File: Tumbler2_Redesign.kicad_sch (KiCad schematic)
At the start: 60 parts, among them J1 Conn_01x04, J2 Conn_01x06, J3 Conn_01x06, J4 USB_C_Receptacle_USB2.0_16P, J5 USB_C_Receptacle_USB2.0_16P, J6 Conn_01x04, Q1 BC817, Q2 BC817, SW1 SW_Push, SW2 SW_Push, SW3 SW_Push, U1 AP63203WU, U2 ESP32-S3-WROOM-1, U3 CP2102N-A02-GQFN28R, U4 AP63205WU, U6 USBLC6-2SC6, U7 USBLC6-2SC6

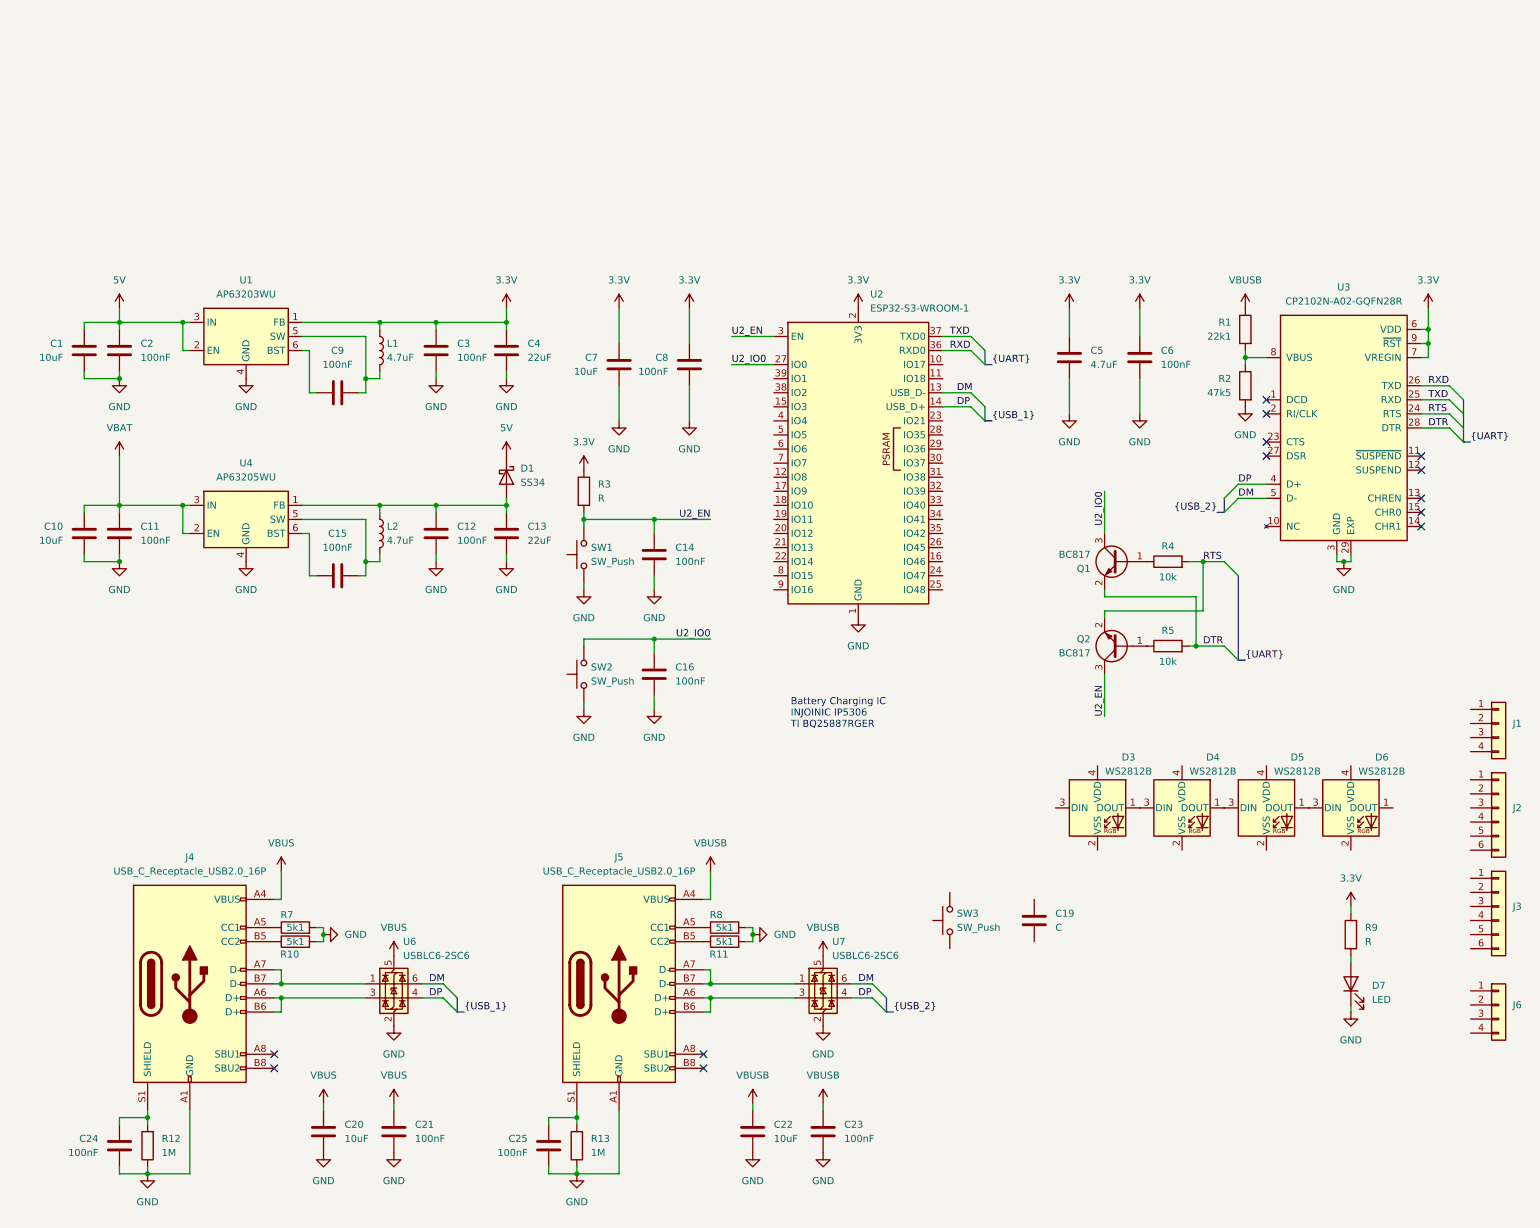
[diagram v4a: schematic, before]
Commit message: Add IMU and motor driver
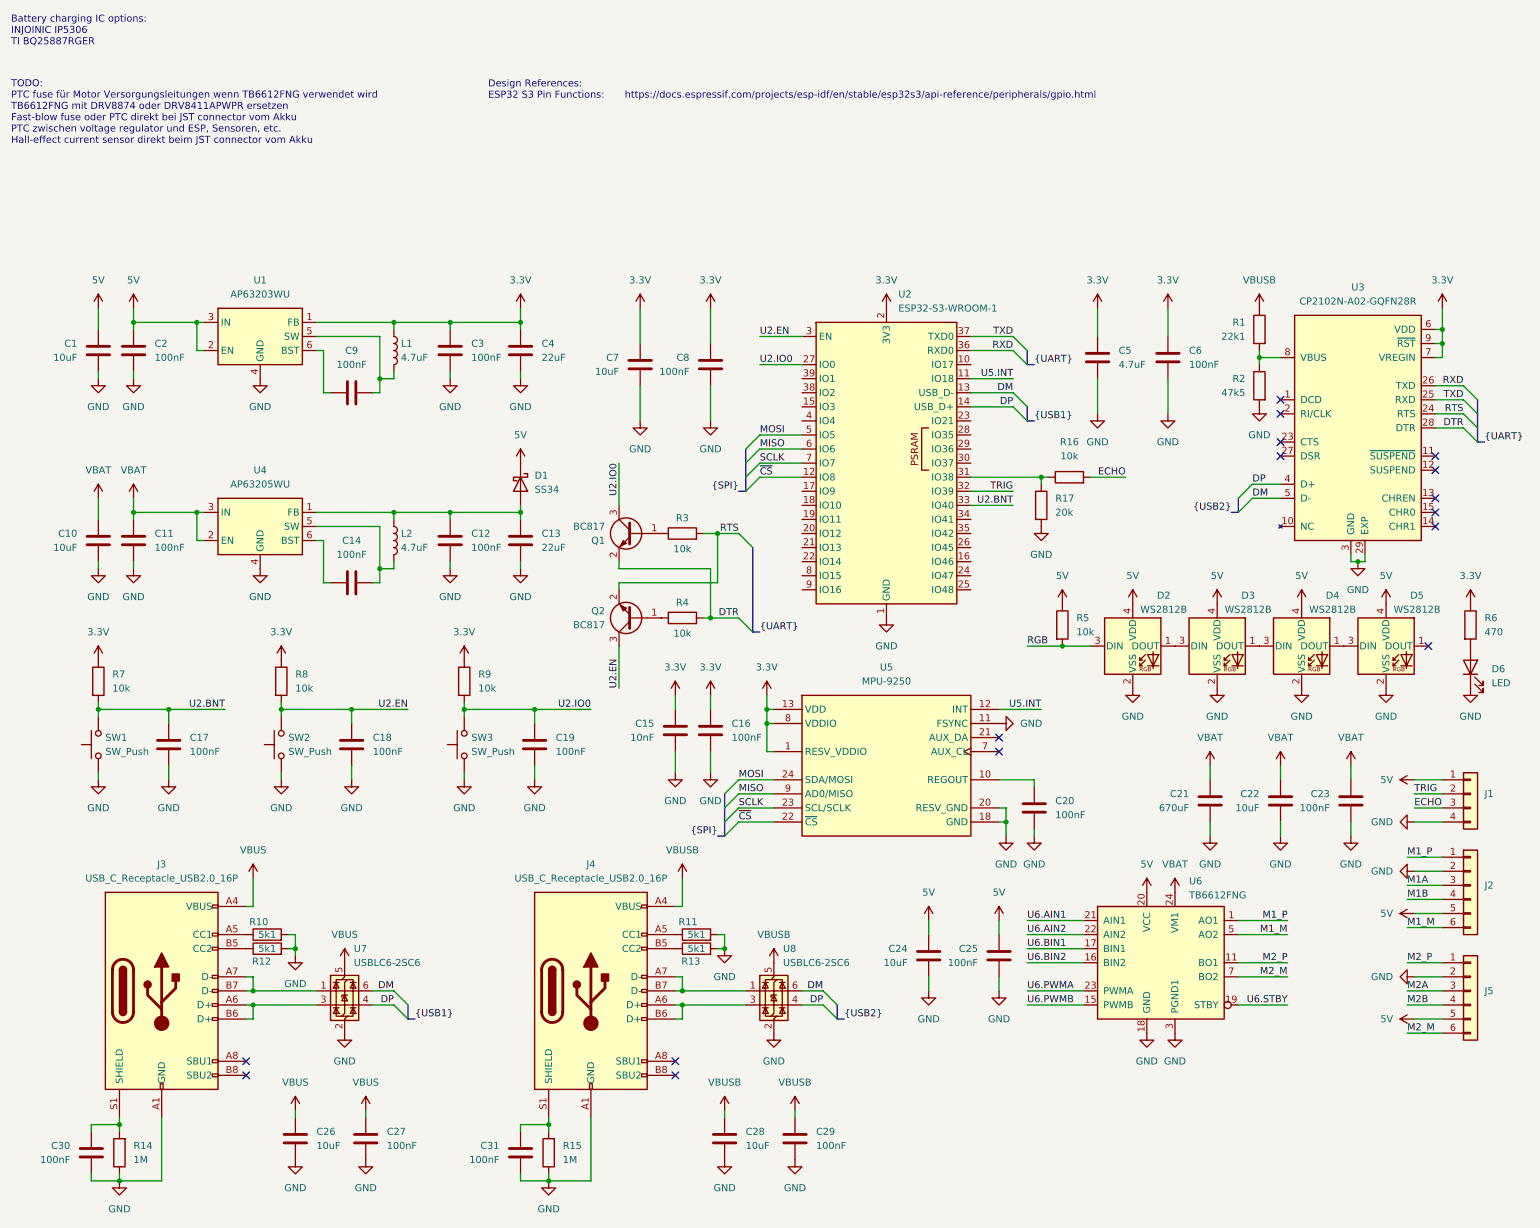
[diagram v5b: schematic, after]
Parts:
- removed C19: C, symbol Device:C
- removed J3: Conn_01x06, symbol Connector_Generic:Conn_01x06
- removed J6: Conn_01x04, symbol Connector_Generic:Conn_01x04
- removed SW3: SW_Push, symbol Switch:SW_Push
- added C15: 10nF, symbol Device:C
- added C16, C17, C20, C23, C25: 100nF, symbol Device:C
- added C21: 670uF, symbol Device:C
- added C22, C24: 10uF, symbol Device:C
- added J5: Conn_01x06, symbol Connector_Generic:Conn_01x06
- added R16, R5, R7, R9: 10k, symbol Device:R
- added R17: 20k, symbol Device:R
- added SW1: SW_Push, symbol Switch:SW_Push
- added U5: MPU-9250, Sensor_Motion:InvenSense_QFN-24_3x3mm_P0.4mm, symbol Sensor_Motion:MPU-9250
- added U6: TB6612FNG, Package_SO:SSOP-24_5.3x8.2mm_P0.65mm, symbol Driver_Motor:TB6612FNG
- D1: LSCS Part No. (none) -> C8678; Product_Link https://www.lcsc.com/product-detail/C8678.html -> (none)
- R6: renamed from R9; value R -> 470
- R8: renamed from R3; value R -> 10k
- U2: LSCS Part No. (none) -> C2913202
- renumbered C15 to C14, C14 to C18, C16 to C19, C20 to C26, C21 to C27, C22 to C28, C23 to C29, C24 to C30, C25 to C31, D3 to D2, D4 to D3, D5 to D4, D6 to D5, D7 to D6, J4 to J3, J5 to J4, R7 to R10, R8 to R11, R10 to R12, R11 to R13, R12 to R14, R13 to R15, R4 to R3, R5 to R4, SW1 to SW2, SW2 to SW3, U6 to U7, U7 to U8
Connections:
- net 3.3V: now also C15.1, C16.1, R7.1, R9.1, U5.1 (RESV_VDDIO), U5.13 (VDD), U5.8 (VDDIO)
- net 5V: now also D2.4 (VDD), D3.4 (VDD), D4.4 (VDD), D5.4 (VDD), J1.1 (Pin_1), J2.5 (Pin_5), C24.1, C25.1, J5.5 (Pin_5), R5.1, U6.20 (VCC)
- net GND: now also D2.2 (VSS), D3.2 (VSS), D4.2 (VSS), D5.2 (VSS), J1.4 (Pin_4), J2.2 (Pin_2), C15.2, C16.2, C17.2, C20.2, C21.2, C22.2, C23.2, C24.2, C25.2, J5.2 (Pin_2), R17.2, SW1.1, U5.11 (FSYNC), U5.18 (GND), U5.20 (RESV_GND), U6.10 (PGND2), U6.18 (GND), U6.3 (PGND1), U6.4 (PGND1), U6.9 (PGND2)
- net VBAT: now also C21.1, C22.1, C23.1, U6.13 (VM2), U6.14 (VM3), U6.24 (VM1)
- net TRIG: now reaches J1.2 (Pin_2)
- net TRIG: now also U2.32 (IO39)
- net ECHO: now reaches J1.3 (Pin_3)
- net ECHO: now also R16.2
- net U5.INT: now reaches U2.11 (IO18)
- net U5.INT: now also U5.12 (INT)
- net ~{CS}: now reaches U2.12 (IO8)
- net ~{CS}: now also U5.22 (~{CS})
- net at U2.31 (IO38): now also R16.1, R17.1
- net U2.BNT: now reaches U2.33 (IO40)
- net U2.BNT: now also C17.1, R7.2, SW1.2
- net MOSI: now reaches U2.5 (IO5)
- net MOSI: now also U5.24 (SDA/MOSI)
- net MISO: now reaches U2.6 (IO6)
- net MISO: now also U5.9 (AD0/MISO)
- net SCLK: now reaches U2.7 (IO7)
- net SCLK: now also U5.23 (SCL/SCLK)
- net RGB: now reaches D2.3 (DIN)
- net RGB: now also R5.2
- net M1_P: now reaches J2.1 (Pin_1)
- net M1_P: now also U6.1 (AO1), U6.2 (AO1)
- net M1A: now reaches J2.3 (Pin_3)
- net M1B: now reaches J2.4 (Pin_4)
- net M1_M: now reaches J2.6 (Pin_6)
- net M1_M: now also U6.5 (AO2), U6.6 (AO2)
- net U2_EN renamed U2.EN
- net U2_IO0 renamed U2.IO0
- net U2.IO0: now also R9.2
- new net: C20.1, U5.10 (REGOUT)
- new net M2A: J5.3 (Pin_3)
- new net M2B: J5.4 (Pin_4)
- new net M2_M: J5.6 (Pin_6), U6.7 (BO2), U6.8 (BO2)
- new net M2_P: J5.1 (Pin_1), U6.11 (BO1), U6.12 (BO1)
- new net U6.AIN1: U6.21 (AIN1)
- new net U6.AIN2: U6.22 (AIN2)
- new net U6.BIN1: U6.17 (BIN1)
- new net U6.BIN2: U6.16 (BIN2)
- new net U6.PWMA: U6.23 (PWMA)
- new net U6.PWMB: U6.15 (PWMB)
- new net U6.STBY: U6.19 (STBY)
- no-connect marks 13 -> 16
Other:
- note added: "Battery charging IC options: INJOINIC IP5306 TI BQ25887RGER"
- note added: "Design References: ESP32 S3 Pin Functions:"
- note added: "TODO: PTC fuse für Motor Versorgungsleitungen wenn TB6612FNG verwendet wird TB6612FNG mit DRV8874 oder DRV8411APWPR ersetzen Fast-blow fuse oder PTC direkt bei JST connector vom Akku PTC zwischen voltage regulator und ESP, Sensoren, etc. Hall-effect current sensor direkt beim JST connector vom Akku"
- note added: "https://docs.espressif.com/projects/esp-idf/en/stable/esp32s3/api-reference/peripherals/gpio.html"
- note removed: "Battery Charging IC INJOINIC IP5306 TI BQ25887RGER"
- moved on the sheet: C1, C10, C11, C12, C13, C14, C18, C19, C2, C26, C27, C28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

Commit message: Move to hierarchical design
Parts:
- removed C1, C10, C22, C24, C26, C28, C7: 10uF, symbol Device:C
- removed C11, C12, C14, C16, C17, C18, C19, C2, C20, C23, C25, C27, C29, C3, C30, C31, C6, C8, C9: 100nF, symbol Device:C
- removed C13, C4: 22uF, symbol Device:C
- removed C15: 10nF, symbol Device:C
- removed C21: 670uF, symbol Device:C
- removed C5: 4.7uF, symbol Device:C
- removed D1: SS34, Diode_SMD:D_SMA, symbol Diode:SS34
- removed D2, D3, D4, D5: WS2812B, LED_SMD:LED_WS2812B-2020_PLCC4_2.0x2.0mm, symbol LED:WS2812B-2020
- removed D6: LED, symbol Device:LED
- removed J1: Conn_01x04, symbol Connector_Generic:Conn_01x04
- removed J2, J5: Conn_01x06, symbol Connector_Generic:Conn_01x06
- removed J3, J4: USB_C_Receptacle_USB2.0_16P, symbol Connector:USB_C_Receptacle_USB2.0_16P
- removed L1, L2: 4.7uF, symbol Device:L
- removed Q1, Q2: BC817, Package_TO_SOT_SMD:SOT-23, symbol Transistor_BJT:BC817
- removed R1: 22k1, symbol Device:R
- removed R10, R11, R12, R13: 5k1, symbol Device:R
- removed R14, R15: 1M, symbol Device:R
- removed R16, R3, R4, R5, R7, R8, R9: 10k, symbol Device:R
- removed R17: 20k, symbol Device:R
- removed R2: 47k5, symbol Device:R
- removed R6: 470, symbol Device:R
- removed SW1, SW2, SW3: SW_Push, symbol Switch:SW_Push
- removed U1: AP63203WU, Package_TO_SOT_SMD:TSOT-23-6, symbol Regulator_Switching:AP63203WU
- removed U2: ESP32-S3-WROOM-1, RF_Module:ESP32-S3-WROOM-1, symbol RF_Module:ESP32-S3-WROOM-1
- removed U3: CP2102N-A02-GQFN28R, Package_DFN_QFN:QFN-28-1EP_5x5mm_P0.5mm_EP3.35x3.35mm, symbol Tumbler2:CP2102N-A02-GQFN28R
- removed U4: AP63205WU, Package_TO_SOT_SMD:TSOT-23-6, symbol Regulator_Switching:AP63205WU
- removed U5: MPU-9250, Sensor_Motion:InvenSense_QFN-24_3x3mm_P0.4mm, symbol Sensor_Motion:MPU-9250
- removed U6: TB6612FNG, Package_SO:SSOP-24_5.3x8.2mm_P0.65mm, symbol Driver_Motor:TB6612FNG
- removed U7, U8: USBLC6-2SC6, Package_TO_SOT_SMD:SOT-23-6, symbol Power_Protection:USBLC6-2SC6
- added H1, H2, H3, H4: MountingHole_Pad, MountingHole:MountingHole_3mm_Pad, symbol Mechanical:MountingHole_Pad
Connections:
- net GND: now also H1.1, H2.1, H3.1, H4.1
- no-connect marks 16 -> 0
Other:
- added sheet MCU (mcu.kicad_sch)
- added sheet Motor Driver (motor_driver.kicad_sch)
- added sheet Pin Headers (pin_headers.kicad_sch)
- added sheet Power Supply (power_supply.kicad_sch)
- added sheet Sensors (sensors.kicad_sch)
- added sheet USB-C Connectors (usb_c_connector.kicad_sch)
- title: (none) -> Tumbler 2 Redesign

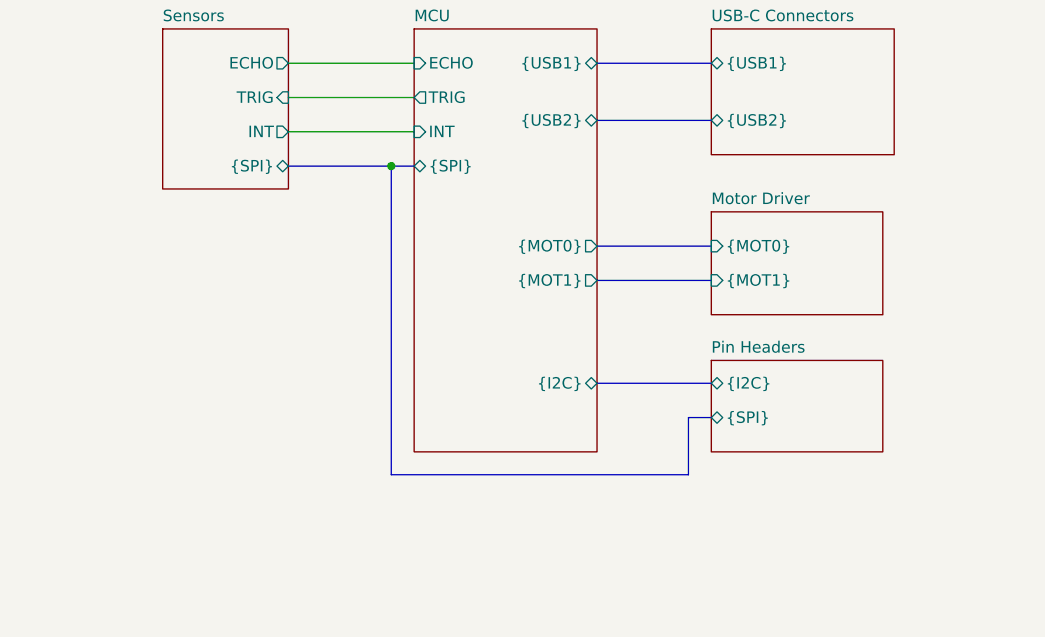
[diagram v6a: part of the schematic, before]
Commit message: Replace schottky with ideal diode
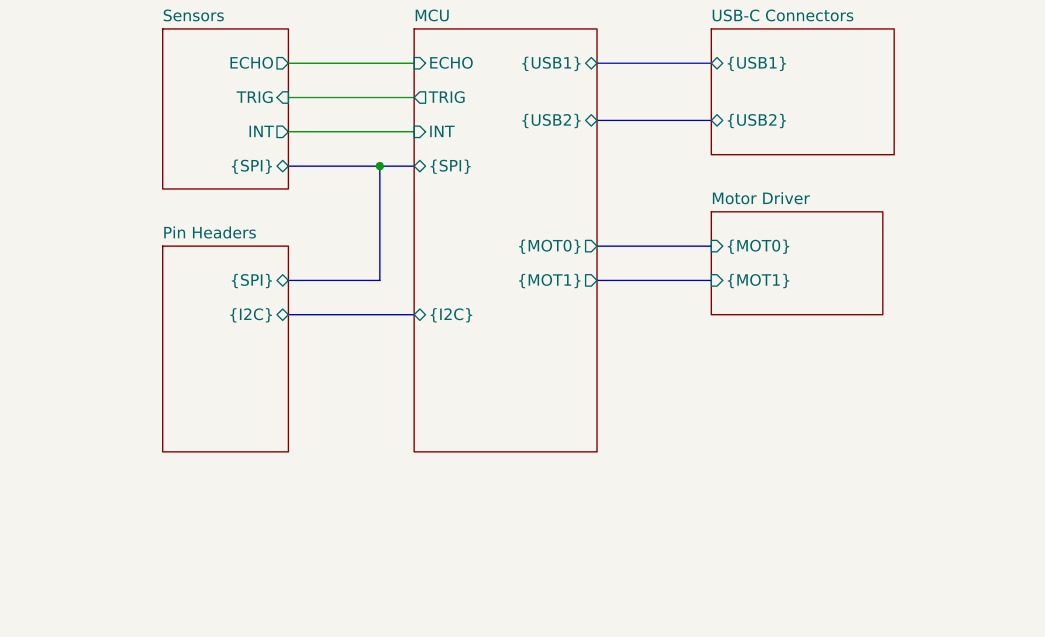
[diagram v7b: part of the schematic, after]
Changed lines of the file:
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@@
 	)
 	(junction
-		(at 130.81 99.06)
+		(at 129.54 99.06)
 		(diameter 0)
 		(color 0 0 0 0)
@@
 	(bus
 		(pts
-			(xy 163.83 133.35) (xy 163.83 127)
+			(xy 129.54 111.76) (xy 129.54 99.06)
 		)
 		(stroke
@@
 	(bus
 		(pts
-			(xy 130.81 99.06) (xy 130.81 133.35)
+			(xy 153.67 107.95) (xy 166.37 107.95)
+		)
+		(stroke
+			(width 0)
+			(type default)
+		)
+	)
+	(wire
+		(pts
+			(xy 119.38 95.25) (xy 133.35 95.25)
 		)
 		(stroke
@@
 	(bus
 		(pts
-			(xy 153.67 107.95) (xy 166.37 107.95)
+			(xy 153.67 93.98) (xy 166.37 93.98)
 		)
 		(stroke
@@
 	(bus
 		(pts
-			(xy 130.81 99.06) (xy 133.35 99.06)
-		)
-		(stroke
-			(width 0)
-			(type default)
-		)
-	)
-	(wire
-		(pts
-			(xy 119.38 95.25) (xy 133.35 95.25)
+			(xy 129.54 99.06) (xy 133.35 99.06)
 		)
 		(stroke
@@
 	(bus
 		(pts
-			(xy 163.83 127) (xy 166.37 127)
+			(xy 119.38 111.76) (xy 129.54 111.76)
 		)
 		(stroke
@@
 	(bus
 		(pts
-			(xy 153.67 93.98) (xy 166.37 93.98)
+			(xy 119.38 99.06) (xy 129.54 99.06)
 		)
 		(stroke
@@
 	(bus
 		(pts
-			(xy 130.81 133.35) (xy 163.83 133.35)
-		)
-		(stroke
-			(width 0)
-			(type default)
-		)
-	)
-	(bus
-		(pts
-			(xy 119.38 99.06) (xy 130.81 99.06)
-		)
-		(stroke
-			(width 0)
-			(type default)
-		)
-	)
-	(bus
-		(pts
-			(xy 153.67 123.19) (xy 166.37 123.19)
+			(xy 119.38 115.57) (xy 133.35 115.57)
 		)
 		(stroke
@@
 		(dnp no)
 		(fields_autoplaced yes)
-		(property "Reference" "#PWR04"
+		(property "Reference" "#PWR029"
 			(at 254 158.75 0)
 			(effects
@@
 			(project "Tumbler2_Redesign"
 				(path "/f3fd8d79-9d35-4c04-811e-2697a2740958"
-					(reference "#PWR04")
+					(reference "#PWR029")
 					(unit 1)
 				)
@@
 		(dnp no)
 		(fields_autoplaced yes)
-		(property "Reference" "#PWR03"
+		(property "Reference" "#PWR028"
 			(at 227.33 158.75 0)
 			(effects
@@
 			(project "Tumbler2_Redesign"
 				(path "/f3fd8d79-9d35-4c04-811e-2697a2740958"
-					(reference "#PWR03")
+					(reference "#PWR028")
 					(unit 1)
 				)
@@
 		(dnp no)
 		(fields_autoplaced yes)
-		(property "Reference" "#PWR02"
+		(property "Reference" "#PWR027"
 			(at 254 144.78 0)
 			(effects
@@
 			(project "Tumbler2_Redesign"
 				(path "/f3fd8d79-9d35-4c04-811e-2697a2740958"
-					(reference "#PWR02")
+					(reference "#PWR027")
 					(unit 1)
 				)
@@
 		(dnp no)
 		(fields_autoplaced yes)
-		(property "Reference" "#PWR01"
+		(property "Reference" "#PWR026"
 			(at 227.33 144.78 0)
 			(effects
@@
 			(project ""
 				(path "/f3fd8d79-9d35-4c04-811e-2697a2740958"
-					(reference "#PWR01")
+					(reference "#PWR026")
 					(unit 1)
 				)
@@
 			(project "Tumbler2_Redesign"
 				(path "/f3fd8d79-9d35-4c04-811e-2697a2740958"
-					(page "1")
+					(page "2")
 				)
 			)
@@
 		)
 		(pin "{I2C}" bidirectional
-			(at 153.67 123.19 0)
-			(effects
-				(font
-					(size 1.27 1.27)
-				)
-				(justify right)
-			)
-		)
-		(instances
-			(project "Tumbler2_Redesign"
-				(path "/f3fd8d79-9d35-4c04-811e-2697a2740958"
-					(page "2")
+			(at 133.35 115.57 180)
+			(effects
+				(font
+					(size 1.27 1.27)
+				)
+				(justify left)
+			)
+		)
+		(instances
+			(project "Tumbler2_Redesign"
+				(path "/f3fd8d79-9d35-4c04-811e-2697a2740958"
+					(page "3")
 				)
 			)
@@
 	)
 	(sheet
-		(at 166.37 120.65)
-		(size 19.05 10.16)
+		(at 105.41 107.95)
+		(size 13.97 22.86)
 		(exclude_from_sim no)
 		(in_bom yes)
@@
 		)
 		(property "Sheetname" "Pin Headers"
-			(at 166.37 119.9384 0)
+			(at 105.41 107.2384 0)
 			(effects
 				(font
@@
 		)
 		(property "Sheetfile" "pin_headers.kicad_sch"
-			(at 166.37 131.3946 0)
+			(at 105.41 131.3946 0)
 			(effects
 				(font
@@
 		)
 		(pin "{I2C}" bidirectional
-			(at 166.37 123.19 180)
-			(effects
-				(font
-					(size 1.27 1.27)
-				)
-				(justify left)
+			(at 119.38 115.57 0)
+			(effects
+				(font
+					(size 1.27 1.27)
+				)
+				(justify right)
 			)
 		)
 		(pin "{SPI}" bidirectional
-			(at 166.37 127 180)
-			(effects
-				(font
-					(size 1.27 1.27)
-				)
-				(justify left)
+			(at 119.38 111.76 0)
+			(effects
+				(font
+					(size 1.27 1.27)
+				)
+				(justify right)
 			)
 		)
@@
 			(project "Tumbler2_Redesign"
 				(path "/f3fd8d79-9d35-4c04-811e-2697a2740958"
-					(page "3")
+					(page "4")
 				)
 			)
@@
 			(project "Tumbler2_Redesign"
 				(path "/f3fd8d79-9d35-4c04-811e-2697a2740958"
-					(page "4")
-				)
-			)
+					(page "6")
+				)
+			)
